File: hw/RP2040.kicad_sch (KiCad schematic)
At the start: 29 parts, among them U5 W25Q128JVSIQ, U6 RP2040, Y1 Crystal_GND24

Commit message: hw: complete routing
Use components available on LCSC.

Signed-off-by: Mahyar Koshkouei <mk@deltabeard.com>
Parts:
- removed TP3: TestPoint, TestPoint:TestPoint_Pad_D1.5mm, symbol Connector:TestPoint
- added TP38, TP39: TestPoint_Small, Project_Specific:TestPoint_Pad_D0.5mm, symbol Connector:TestPoint_Small
- C13, C14, C27: value 2.2u -> 1u; LCSC C23630 -> C15849
- TP2, TP4, TP5, TP6, TP7, TP8: footprint TestPoint:TestPoint_Pad_D1.5mm -> TestPoint:TestPoint_Pad_D1.0mm
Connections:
- net DATA_DIR: now also TP39.1
- net RUN: now also TP38.1
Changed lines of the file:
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@@
     (comment 2 "Compatible with DMG, MGB, & CGB. Collectively referred to as \"GB\" here.")
   )
+  (junction (at 70.485 127.635) (diameter 0.9144) (color 0 0 0 0))
   (junction (at 75.565 109.22) (diameter 0.9144) (color 0 0 0 0))
   (junction (at 77.47 57.785) (diameter 0.9144) (color 0 0 0 0))
@@
   (junction (at 189.865 34.29) (diameter 0.9144) (color 0 0 0 0))
   (junction (at 189.865 39.37) (diameter 0.9144) (color 0 0 0 0))
+  (junction (at 194.31 148.59) (diameter 0.9144) (color 0 0 0 0))
   (junction (at 200.025 34.29) (diameter 0.9144) (color 0 0 0 0))
   (junction (at 200.025 39.37) (diameter 0.9144) (color 0 0 0 0))
@@
     (stroke (width 0) (type solid) (color 0 0 0 0))
   )
-  (wire (pts (xy 50.8 27.94) (xy 55.88 27.94))
-    (stroke (width 0) (type solid) (color 0 0 0 0))
-  )
   (wire (pts (xy 54.61 76.2) (xy 64.77 76.2))
     (stroke (width 0) (type solid) (color 0 0 0 0))
@@
     (stroke (width 0) (type solid) (color 0 0 0 0))
   )
-  (wire (pts (xy 55.88 27.94) (xy 55.88 29.21))
-    (stroke (width 0) (type solid) (color 0 0 0 0))
-  )
   (wire (pts (xy 65.405 123.825) (xy 65.405 127.635))
     (stroke (width 0) (type solid) (color 0 0 0 0))
   )
-  (wire (pts (xy 65.405 127.635) (xy 75.565 127.635))
+  (wire (pts (xy 65.405 127.635) (xy 70.485 127.635))
     (stroke (width 0) (type solid) (color 0 0 0 0))
   )
@@
     (stroke (width 0) (type solid) (color 0 0 0 0))
   )
+  (wire (pts (xy 70.485 127.635) (xy 75.565 127.635))
+    (stroke (width 0) (type solid) (color 0 0 0 0))
+  )
   (wire (pts (xy 75.565 104.14) (xy 75.565 109.22))
     (stroke (width 0) (type solid) (color 0 0 0 0))
@@
     (stroke (width 0) (type solid) (color 0 0 0 0))
   )
-  (wire (pts (xy 195.58 148.59) (xy 191.77 148.59))
+  (wire (pts (xy 194.31 148.59) (xy 191.77 148.59))
+    (stroke (width 0) (type solid) (color 0 0 0 0))
+  )
+  (wire (pts (xy 195.58 148.59) (xy 194.31 148.59))
     (stroke (width 0) (type solid) (color 0 0 0 0))
   )
@@
     )
   )
+  (symbol (lib_id "Connector:TestPoint_Small") (at 70.485 127.635 0) (unit 1)
+    (in_bom yes) (on_board yes) (fields_autoplaced)
+    (property "Reference" "TP38" (id 0) (at 72.39 127.6349 0)
+      (effects (font (size 1.27 1.27)) (justify left) hide)
+    )
+    (property "Value" "TestPoint_Small" (id 1) (at 70.485 125.603 0)
+      (effects (font (size 1.27 1.27)) hide)
+    )
+    (property "Footprint" "Project_Specific:TestPoint_Pad_D0.5mm" (id 2) (at 75.565 127.635 0)
+      (effects (font (size 1.27 1.27)) hide)
+    )
+    (property "Datasheet" "~" (id 3) (at 75.565 127.635 0)
+      (effects (font (size 1.27 1.27)) hide)
+    )
+    (pin "1")
+  )
   (symbol (lib_id "Connector:TestPoint_Small") (at 111.76 133.35 0) (unit 1)
     (in_bom yes) (on_board yes)
@@
       (effects (font (size 1.27 1.27)) hide)
     )
-    (property "Footprint" "TestPoint:TestPoint_Pad_D1.5mm" (id 2) (at 116.84 133.35 0)
+    (property "Footprint" "TestPoint:TestPoint_Pad_D1.0mm" (id 2) (at 116.84 133.35 0)
       (effects (font (size 1.27 1.27)) hide)
     )
@@
       (effects (font (size 1.27 1.27)) hide)
     )
-    (property "Footprint" "TestPoint:TestPoint_Pad_D1.5mm" (id 2) (at 116.84 135.89 0)
+    (property "Footprint" "TestPoint:TestPoint_Pad_D1.0mm" (id 2) (at 116.84 135.89 0)
       (effects (font (size 1.27 1.27)) hide)
     )
@@
       (effects (font (size 1.27 1.27)) hide)
     )
-    (property "Footprint" "TestPoint:TestPoint_Pad_D1.5mm" (id 2) (at 116.84 138.43 0)
+    (property "Footprint" "TestPoint:TestPoint_Pad_D1.0mm" (id 2) (at 116.84 138.43 0)
       (effects (font (size 1.27 1.27)) hide)
     )
     (property "Datasheet" "~" (id 3) (at 116.84 138.43 0)
+      (effects (font (size 1.27 1.27)) hide)
+    )
+    (pin "1")
+  )
+  (symbol (lib_id "Connector:TestPoint_Small") (at 194.31 148.59 0) (unit 1)
+    (in_bom yes) (on_board yes) (fields_autoplaced)
+    (property "Reference" "TP39" (id 0) (at 196.215 148.5899 0)
+      (effects (font (size 1.27 1.27)) (justify left) hide)
+    )
+    (property "Value" "TestPoint_Small" (id 1) (at 194.31 146.558 0)
+      (effects (font (size 1.27 1.27)) hide)
+    )
+    (property "Footprint" "Project_Specific:TestPoint_Pad_D0.5mm" (id 2) (at 199.39 148.59 0)
+      (effects (font (size 1.27 1.27)) hide)
+    )
+    (property "Datasheet" "~" (id 3) (at 199.39 148.59 0)
       (effects (font (size 1.27 1.27)) hide)
     )
@@
     (property "Reference" "TP2" (id 0) (at 43.2435 25.4 90))
     (property "Value" "TestPoint" (id 1) (at 47.6885 22.225 90))
-    (property "Footprint" "TestPoint:TestPoint_Pad_D1.5mm" (id 2) (at 50.8 20.32 0)
+    (property "Footprint" "TestPoint:TestPoint_Pad_D1.0mm" (id 2) (at 50.8 20.32 0)
       (effects (font (size 1.27 1.27)) hide)
     )
     (property "Datasheet" "~" (id 3) (at 50.8 20.32 0)
-      (effects (font (size 1.27 1.27)) hide)
-    )
-    (pin "1")
-  )
-  (symbol (lib_id "Connector:TestPoint") (at 50.8 27.94 90) (unit 1)
-    (in_bom yes) (on_board yes)
-    (property "Reference" "TP3" (id 0) (at 43.2435 27.94 90))
-    (property "Value" "TestPoint" (id 1) (at 48.3235 29.845 90))
-    (property "Footprint" "TestPoint:TestPoint_Pad_D1.5mm" (id 2) (at 50.8 22.86 0)
-      (effects (font (size 1.27 1.27)) hide)
-    )
-    (property "Datasheet" "~" (id 3) (at 50.8 22.86 0)
       (effects (font (size 1.27 1.27)) hide)
     )
@@
     (property "Reference" "TP4" (id 0) (at 87.0585 24.765 90))
     (property "Value" "TestPoint" (id 1) (at 91.5035 22.225 90))
-    (property "Footprint" "TestPoint:TestPoint_Pad_D1.5mm" (id 2) (at 94.615 19.685 0)
+    (property "Footprint" "TestPoint:TestPoint_Pad_D1.0mm" (id 2) (at 94.615 19.685 0)
       (effects (font (size 1.27 1.27)) hide)
     )
@@
     (property "Reference" "TP5" (id 0) (at 87.0585 29.845 90))
     (property "Value" "TestPoint" (id 1) (at 91.5035 32.385 90))
-    (property "Footprint" "TestPoint:TestPoint_Pad_D1.5mm" (id 2) (at 94.615 24.765 0)
+    (property "Footprint" "TestPoint:TestPoint_Pad_D1.0mm" (id 2) (at 94.615 24.765 0)
       (effects (font (size 1.27 1.27)) hide)
     )
     (property "Datasheet" "~" (id 3) (at 94.615 24.765 0)
-      (effects (font (size 1.27 1.27)) hide)
-    )
-    (pin "1")
-  )
-  (symbol (lib_id "power:GND") (at 55.88 29.21 0) (unit 1)
-    (in_bom yes) (on_board yes) (fields_autoplaced)
-    (property "Reference" "#PWR028" (id 0) (at 55.88 35.56 0)
-      (effects (font (size 1.27 1.27)) hide)
-    )
-    (property "Value" "GND" (id 1) (at 55.88 33.7726 0))
-    (property "Footprint" "" (id 2) (at 55.88 29.21 0)
-      (effects (font (size 1.27 1.27)) hide)
-    )
-    (property "Datasheet" "" (id 3) (at 55.88 29.21 0)
       (effects (font (size 1.27 1.27)) hide)
     )
@@
       (effects (font (size 1.27 1.27)) (justify left))
     )
-    (property "Value" "2.2u" (id 1) (at 85.979 62.992 0)
+    (property "Value" "1u" (id 1) (at 85.979 62.992 0)
       (effects (font (size 1.27 1.27)) (justify left))
     )
@@
       (effects (font (size 1.27 1.27)) hide)
     )
-    (property "LCSC" "C23630" (id 4) (at 85.725 60.96 0)
+    (property "LCSC" "C15849" (id 4) (at 85.725 60.96 0)
       (effects (font (size 1.27 1.27)) hide)
     )
@@
       (effects (font (size 1.27 1.27)) (justify left))
     )
-    (property "Value" "2.2u" (id 1) (at 142.494 38.862 0)
+    (property "Value" "1u" (id 1) (at 142.494 38.862 0)
       (effects (font (size 1.27 1.27)) (justify left))
     )
@@
       (effects (font (size 1.27 1.27)) hide)
     )
-    (property "LCSC" "C23630" (id 4) (at 142.24 36.83 0)
+    (property "LCSC" "C15849" (id 4) (at 142.24 36.83 0)
       (effects (font (size 1.27 1.27)) hide)
     )
@@
       (effects (font (size 1.27 1.27)) (justify left))
     )
-    (property "Value" "2.2u" (id 1) (at 156.464 40.132 0)
+    (property "Value" "1u" (id 1) (at 156.464 40.132 0)
       (effects (font (size 1.27 1.27)) (justify left))
     )
@@
       (effects (font (size 1.27 1.27)) hide)
     )
-    (property "LCSC" "C23630" (id 4) (at 156.21 38.1 0)
-      (effects (font (size 1.27 1.27)) hide)
-    )
+    (property "LCSC" "C15849" (id 4) (at 156.21 38.1 0)
+      (effects (font (size 1.27 1.27)) hide)
+    )

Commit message: hw: add more information to BOM
Signed-off-by: Mahyar Koshkouei <mk@deltabeard.com>
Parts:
- C10, C9: MFr (none) -> CL10C300JB8NNNC; Manufacturer (none) -> Samsung Electro-Mechanics; Notes (none) -> Alternative manufacturer is acceptable
- C11, C12, C15, C16, C17, C18, C19, C20, C26: MFr (none) -> CL05B104KO5NNNC; Manufacturer (none) -> Samsung Electro-Mechanics; Notes (none) -> Alternative manufacturer is acceptable
- C13, C14, C27: MFr (none) -> CL10A105KB8NNNC; Manufacturer (none) -> Samsung Electro-Mechanics; Notes (none) -> Alternative manufacturer is acceptable
- R3: MFr (none) -> 0603WAF1003T5E; Manufacturer (none) -> UNI-ROYAL(Uniroyal Elec); Notes (none) -> Alternative manufacturer is acceptable
- R4, R5: MFr (none) -> 0603WAF1001T5E; Manufacturer (none) -> UNI-ROYAL(Uniroyal Elec); Notes (none) -> Alternative manufacturer is acceptable
- R6, R7: MFr (none) -> 0603WAF270JT5E; Manufacturer (none) -> UNI-ROYAL(Uniroyal Elec); Notes (none) -> Alternative manufacturer is acceptable
- TP2, TP38, TP39, TP4, TP5, TP6, TP7, TP8: Notes (none) -> Only footprint, no component.
- U5: MFr (none) -> W25Q128JVSIQ; Manufacturer (none) -> Winbond Elec; Notes (none) -> Do not populate.
- U6: Manufacturer (none) -> Raspberry Pi
- Y1: MFr (none) -> X322512MSB4SI; Manufacturer (none) -> Yangxing Tech

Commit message: hw: fix USB
Additionally reduced the size of the battery holder.

Signed-off-by: Mahyar Koshkouei <mk@deltabeard.com>
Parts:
- R7: Manufacturer UNI-ROYAL(Uniroyal Elec) -> UNI-ROYAL(Uniroyal Elec)
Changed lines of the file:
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@@
       (effects (font (size 1.27 1.27)) hide)
     )
-    (property "Manufacturer" " UNI-ROYAL(Uniroyal Elec) " (id 8) (at 191.77 60.96 0)
+    (property "Manufacturer" "UNI-ROYAL(Uniroyal Elec) " (id 8) (at 191.77 60.96 0)
       (effects (font (size 1.27 1.27)) hide)
     )

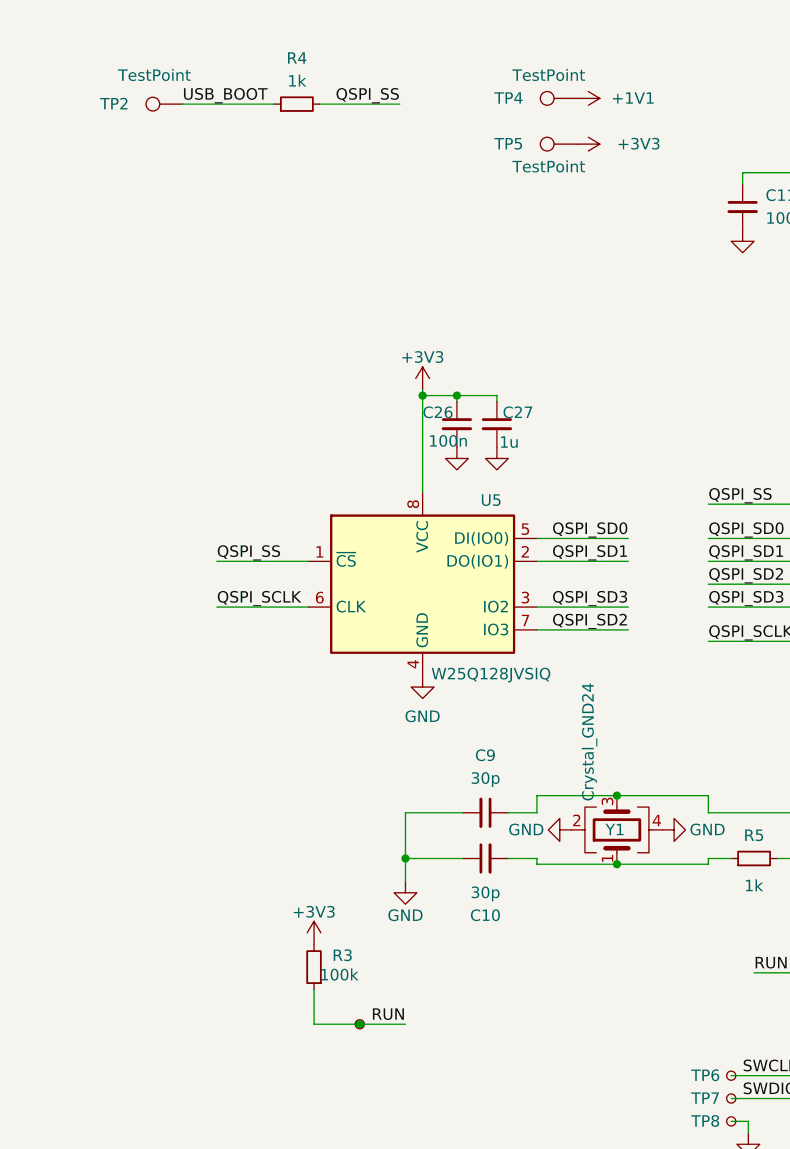
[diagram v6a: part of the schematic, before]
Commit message: hw: add BOOTSEL button and routing changes
Signed-off-by: Mahyar Koshkouei <mk@deltabeard.com>
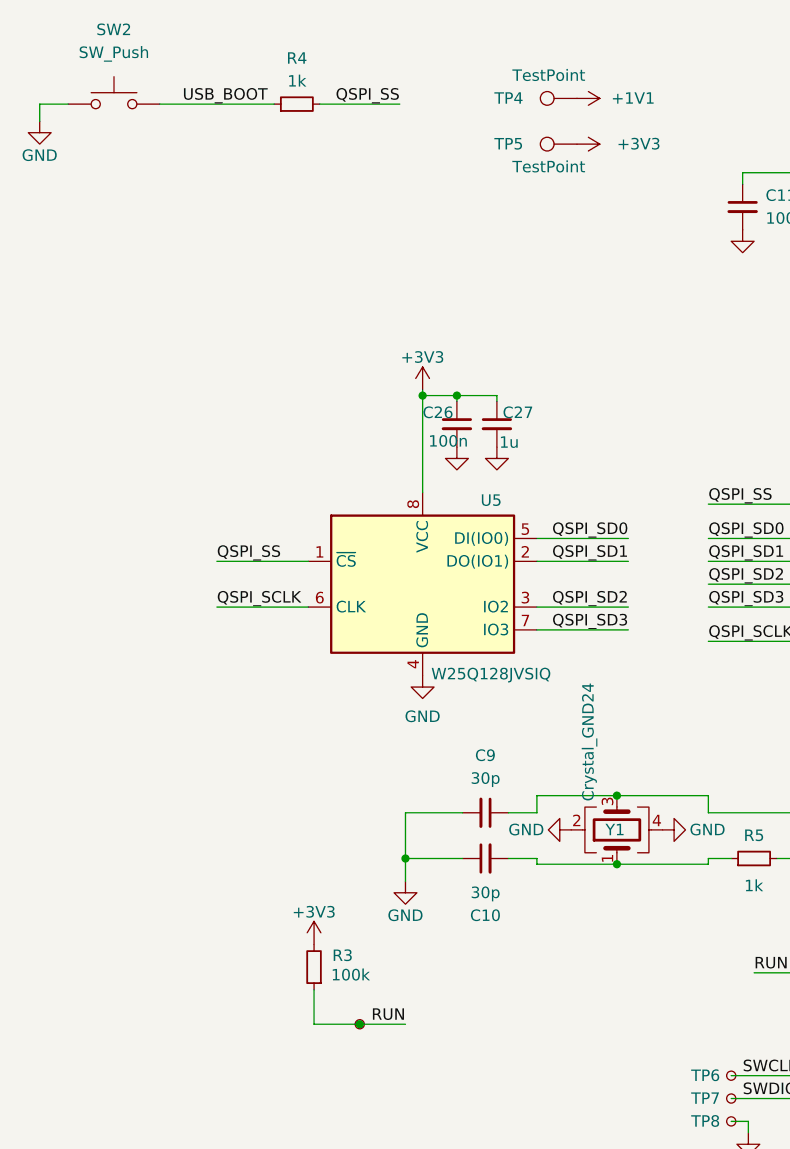
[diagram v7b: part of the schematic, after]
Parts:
- removed TP2: TestPoint, TestPoint:TestPoint_Pad_D1.0mm, symbol Connector:TestPoint
- added SW2: SW_Push, Button_Switch_SMD:SW_SPST_CK_RS282G05A3, symbol Switch:SW_Push
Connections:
- net GND: now also SW2.1
- net QSPI_SD2: now also U5.3 (IO2); no longer U5.7 (IO3)
- net QSPI_SD3: now also U5.7 (IO3); no longer U5.3 (IO2)
- net USB_BOOT: now also SW2.2
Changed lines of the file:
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@@
   (title_block
     (title "RP2040 Game Boy Cart")
-    (date "2021-08-31")
-    (rev "0.2a")
+    (date "2021-09-29")
+    (rev "0.3a")
     (company "Mahyar Koshkouei")
     (comment 1 "All Rights Reserved")
@@
     (stroke (width 0) (type solid) (color 0 0 0 0))
   )
-  (wire (pts (xy 50.8 25.4) (xy 60.96 25.4))
+  (wire (pts (xy 34.925 25.4) (xy 34.925 27.305))
+    (stroke (width 0) (type default) (color 0 0 0 0))
+  )
+  (wire (pts (xy 38.1 25.4) (xy 34.925 25.4))
+    (stroke (width 0) (type default) (color 0 0 0 0))
+  )
+  (wire (pts (xy 48.26 25.4) (xy 60.96 25.4))
     (stroke (width 0) (type solid) (color 0 0 0 0))
   )
@@
     (effects (font (size 1.27 1.27)) (justify right bottom))
   )
-  (label "QSPI_SD3" (at 100.33 81.28 180)
-    (effects (font (size 1.27 1.27)) (justify right bottom))
-  )
-  (label "QSPI_SD2" (at 100.33 83.82 180)
+  (label "QSPI_SD2" (at 100.33 81.28 180)
+    (effects (font (size 1.27 1.27)) (justify right bottom))
+  )
+  (label "QSPI_SD3" (at 100.33 83.82 180)
     (effects (font (size 1.27 1.27)) (justify right bottom))
   )
@@
     )
     (property "Datasheet" "" (id 3) (at 163.83 27.94 0)
-      (effects (font (size 1.27 1.27)) hide)
-    )
-    (pin "1")
-  )
-  (symbol (lib_id "Connector:TestPoint") (at 50.8 25.4 90) (unit 1)
-    (in_bom yes) (on_board yes)
-    (property "Reference" "TP2" (id 0) (at 43.2435 25.4 90))
-    (property "Value" "TestPoint" (id 1) (at 47.6885 22.225 90))
-    (property "Footprint" "TestPoint:TestPoint_Pad_D1.0mm" (id 2) (at 50.8 20.32 0)
-      (effects (font (size 1.27 1.27)) hide)
-    )
-    (property "Datasheet" "~" (id 3) (at 50.8 20.32 0)
-      (effects (font (size 1.27 1.27)) hide)
-    )
-    (property "Notes" "Only footprint, no component." (id 4) (at 50.8 25.4 0)
       (effects (font (size 1.27 1.27)) hide)
     )
@@
     (pin "1")
   )
+  (symbol (lib_id "power:GND") (at 34.925 27.305 0) (unit 1)
+    (in_bom yes) (on_board yes) (fields_autoplaced)
+    (property "Reference" "#PWR0103" (id 0) (at 34.925 33.655 0)
+      (effects (font (size 1.27 1.27)) hide)
+    )
+    (property "Value" "GND" (id 1) (at 34.925 31.115 0))
+    (property "Footprint" "" (id 2) (at 34.925 27.305 0)
+      (effects (font (size 1.27 1.27)) hide)
+    )
+    (property "Datasheet" "" (id 3) (at 34.925 27.305 0)
+      (effects (font (size 1.27 1.27)) hide)
+    )
+    (pin "1")
+  )
   (symbol (lib_id "power:GND") (at 75.565 111.76 0) (unit 1)
     (in_bom yes) (on_board yes) (fields_autoplaced)
@@
     (in_bom yes) (on_board yes)
     (property "Reference" "R3" (id 0) (at 68.58 120.015 0))
-    (property "Value" "100k" (id 1) (at 70.358 122.174 0)
+    (property "Value" "100k" (id 1) (at 71.628 122.174 0)
       (effects (font (size 1.27 1.27)) (justify left))
     )
@@
       (effects (font (size 1.27 1.27)) hide)
     )
+    (pin "1")
+    (pin "2")
+  )
+  (symbol (lib_id "Switch:SW_Push") (at 43.18 25.4 0) (unit 1)
+    (in_bom yes) (on_board yes) (fields_autoplaced)
+    (property "Reference" "SW2" (id 0) (at 43.18 17.145 0))
+    (property "Value" "SW_Push" (id 1) (at 43.18 19.685 0))
+    (property "Footprint" "Button_Switch_SMD:SW_SPST_CK_RS282G05A3" (id 2) (at 43.18 20.32 0)
+      (effects (font (size 1.27 1.27)) hide)
+    )
+    (property "Datasheet" "~" (id 3) (at 43.18 20.32 0)
+      (effects (font (size 1.27 1.27)) hide)
+    )
+    (property "LCSC" "C557591" (id 4) (at 43.18 25.4 0)
+      (effects (font (size 1.27 1.27)) hide)
+    )

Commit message: hw: use CR2032 footprint & larger testpoints
Signed-off-by: Mahyar Koshkouei <mk@deltabeard.com>
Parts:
- TP38, TP39: footprint Project_Specific:TestPoint_Pad_D0.5mm -> TestPoint:TestPoint_Pad_D1.0mm
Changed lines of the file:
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@@
       (effects (font (size 1.27 1.27)) hide)
     )
-    (property "Footprint" "Project_Specific:TestPoint_Pad_D0.5mm" (id 2) (at 75.565 127.635 0)
+    (property "Footprint" "TestPoint:TestPoint_Pad_D1.0mm" (id 2) (at 75.565 127.635 0)
       (effects (font (size 1.27 1.27)) hide)
     )
@@
       (effects (font (size 1.27 1.27)) hide)
     )
-    (property "Footprint" "Project_Specific:TestPoint_Pad_D0.5mm" (id 2) (at 199.39 148.59 0)
+    (property "Footprint" "TestPoint:TestPoint_Pad_D1.0mm" (id 2) (at 199.39 148.59 0)
       (effects (font (size 1.27 1.27)) hide)
     )
